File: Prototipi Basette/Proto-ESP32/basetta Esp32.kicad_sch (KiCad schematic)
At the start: 32 parts, among them J1 Conn_01x19, J2 Conn_01x19, J3 Conn_01x19, J4 Conn_01x19, J5 Screw_Terminal_01x02, J6 Conn_01x05, J7 Conn_01x02, Q1 BC547, Q2 BC547, Q3 IRF9540N, Q4 BC547, Q5 BC557, SW1 RESET, SW2 SET, U3 4013

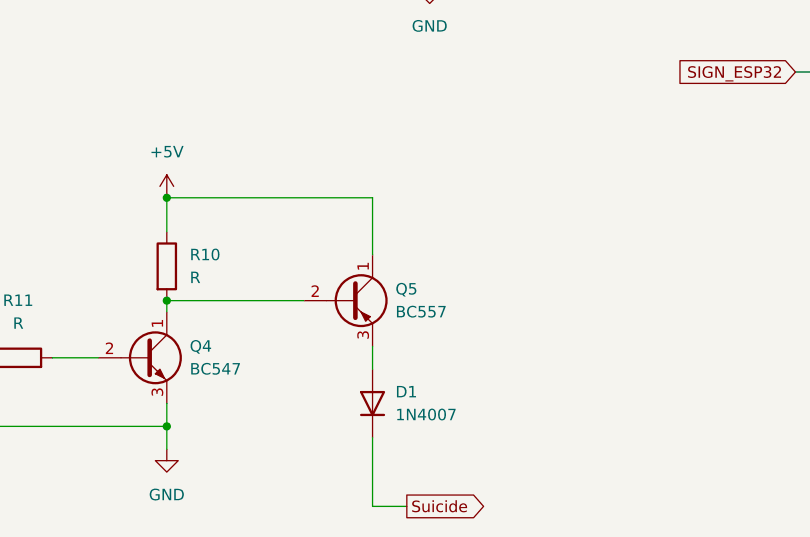
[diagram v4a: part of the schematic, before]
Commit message: Add Primo Circuito KiCad project; update ESP32 PCB
Add a new KiCad project "Primo Circuito KiCad": schematic (.kicad_sch), board file (.kicad_pcb), project/settings (.kicad_pro, .kicad_prl) and a PDF export (BERNARDIS.pdf). The schematic contains a simple BJT/LED prototype and power symbols. Also update Proto-ESP32: add Basetta_ESP32.zip and a dated backup under basetta Esp32-backups/, remove Gerber.zip, and apply updates to basetta Esp32 KiCad files (.kicad_pcb, .kicad_prl, .kicad_pro, .kicad_sch).
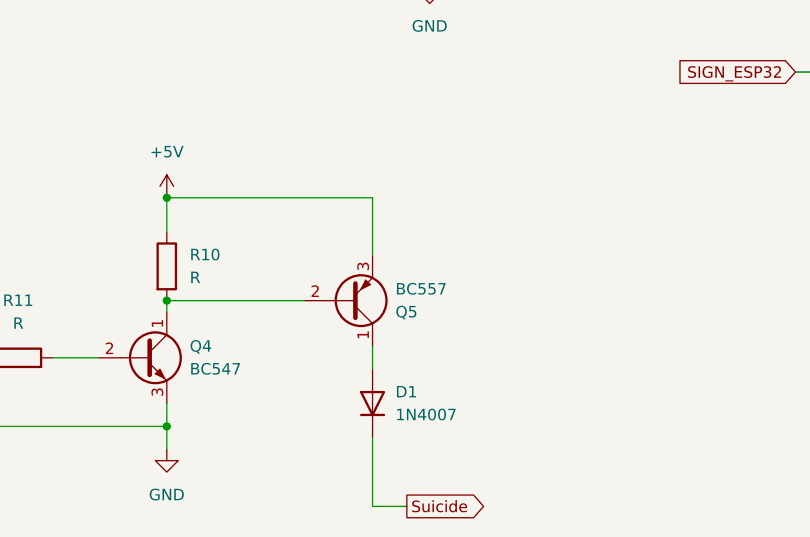
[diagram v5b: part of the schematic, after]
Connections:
- net +5V: now also Q5.3 (E); no longer Q5.1 (C)
- net at D1.2 (A): now also Q5.1 (C); no longer Q5.3 (E)
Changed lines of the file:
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@@
 	)
 	(junction
+		(at 160.02 137.16)
+		(diameter 0)
+		(color 0 0 0 0)
+	)
+	(junction
 		(at 44.45 30.48)
 		(diameter 0)
@@
 	)
 	(junction
-		(at 160.02 137.16)
-		(diameter 0)
-		(color 0 0 0 0)
-	)
-	(junction
 		(at 250.19 111.76)
 		(diameter 0)
@@
 	(wire
 		(pts
+			(xy 160.02 137.16) (xy 175.26 137.16)
+		)
+		(stroke
+			(width 0)
+			(type default)
+		)
+	)
+	(wire
+		(pts
 			(xy 181.61 39.37) (xy 203.2 39.37)
 		)
@@
 	(wire
 		(pts
-			(xy 182.88 144.78) (xy 182.88 142.24)
+			(xy 160.02 138.43) (xy 160.02 137.16)
 		)
 		(stroke
@@
 	(wire
 		(pts
-			(xy 160.02 138.43) (xy 160.02 137.16)
+			(xy 189.23 85.09) (xy 180.34 85.09)
 		)
 		(stroke
@@
 	(wire
 		(pts
-			(xy 189.23 85.09) (xy 180.34 85.09)
+			(xy 100.33 50.8) (xy 111.76 50.8)
 		)
 		(stroke
@@
 	(wire
 		(pts
-			(xy 100.33 50.8) (xy 111.76 50.8)
+			(xy 100.33 55.88) (xy 111.76 55.88)
 		)
 		(stroke
@@
 	(wire
 		(pts
-			(xy 100.33 55.88) (xy 111.76 55.88)
+			(xy 33.02 58.42) (xy 44.45 58.42)
 		)
 		(stroke
@@
 	(wire
 		(pts
-			(xy 33.02 58.42) (xy 44.45 58.42)
+			(xy 33.02 30.48) (xy 44.45 30.48)
 		)
 		(stroke
@@
 	(wire
 		(pts
-			(xy 33.02 30.48) (xy 44.45 30.48)
+			(xy 250.19 93.98) (xy 260.35 93.98)
 		)
 		(stroke
@@
 	(wire
 		(pts
-			(xy 250.19 93.98) (xy 260.35 93.98)
+			(xy 182.88 125.73) (xy 182.88 132.08)
 		)
 		(stroke
@@
 	(wire
 		(pts
-			(xy 160.02 137.16) (xy 175.26 137.16)
-		)
-		(stroke
-			(width 0)
-			(type default)
-		)
-	)
-	(wire
-		(pts
 			(xy 33.02 63.5) (xy 44.45 63.5)
 		)
@@
 	(wire
 		(pts
-			(xy 182.88 132.08) (xy 182.88 125.73)
-		)
-		(stroke
-			(width 0)
-			(type default)
-		)
-	)
-	(wire
-		(pts
 			(xy 193.04 46.99) (xy 193.04 49.53)
 		)
@@
 	(wire
 		(pts
+			(xy 182.88 142.24) (xy 182.88 144.78)
+		)
+		(stroke
+			(width 0)
+			(type default)
+		)
+	)
+	(wire
+		(pts
 			(xy 175.26 67.31) (xy 179.07 67.31)
 		)
@@
 		(lib_id "Transistor_BJT:BC557")
 		(at 180.34 137.16 0)
+		(mirror x)
 		(unit 1)
 		(body_style 1)
@@
 		(in_pos_files yes)
 		(dnp no)
-		(fields_autoplaced yes)
 		(property "Reference" "Q5"
-			(at 185.42 135.8899 0)
+			(at 185.42 138.4301 0)
 			(show_name no)
 			(do_not_autoplace no)
@@
 		)
 		(property "Value" "BC557"
-			(at 185.42 138.4299 0)
+			(at 185.42 135.8901 0)
 			(show_name no)
 			(do_not_autoplace no)
@@
 		)
 		(property "Footprint" "Package_TO_SOT_THT:TO-92_Inline"
-			(at 185.42 139.065 0)
+			(at 185.42 135.255 0)
 			(hide yes)
 			(show_name no)
